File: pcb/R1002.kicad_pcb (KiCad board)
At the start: 2 copper layers, 45 x 33.3 mm, 11 parts, among them J1 PCIEXPRESS-X1, J2 CONN_01X04, J3 CONN_01X04, Q1 Q_NMOS_GDSD, Q2 Q_NMOS_GDSD, Q3 Q_NMOS_GDSD, Q4 Q_NMOS_GDSD, U1 MC14504B-TSSOP

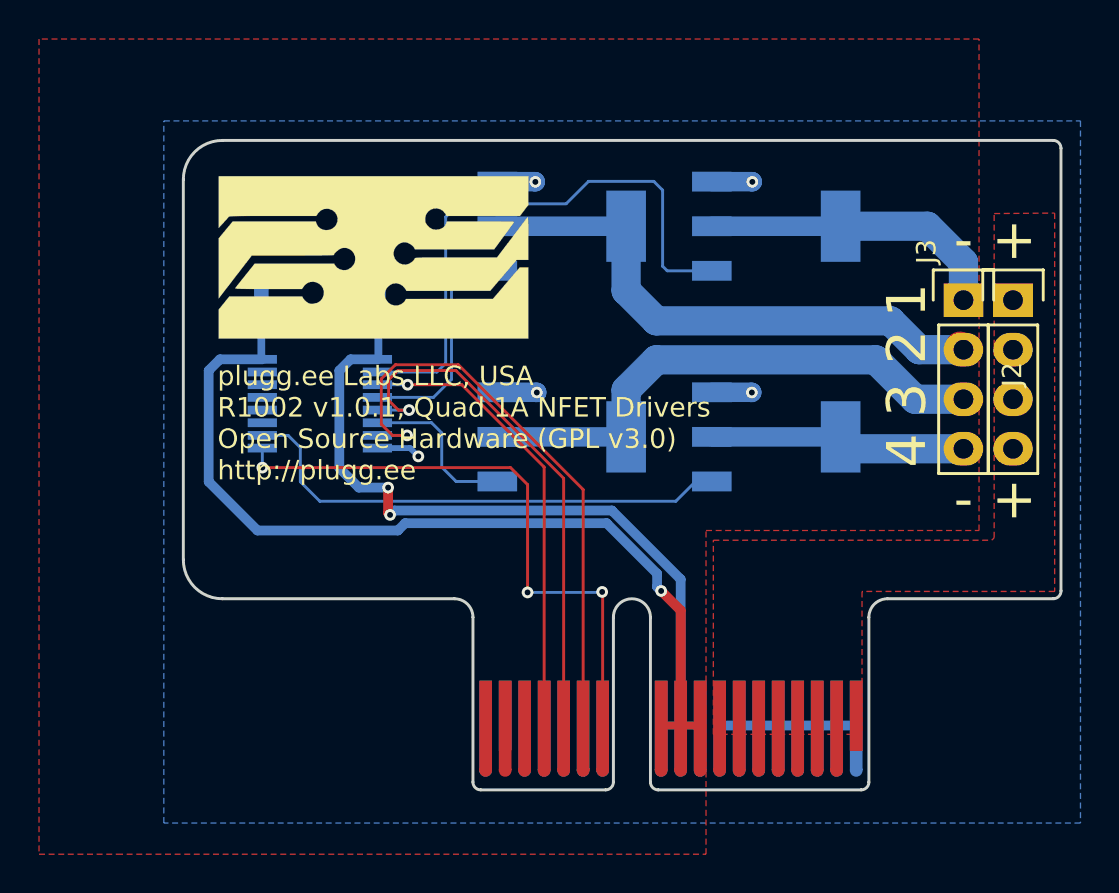
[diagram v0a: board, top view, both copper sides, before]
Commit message: added fiducials, exported BOM
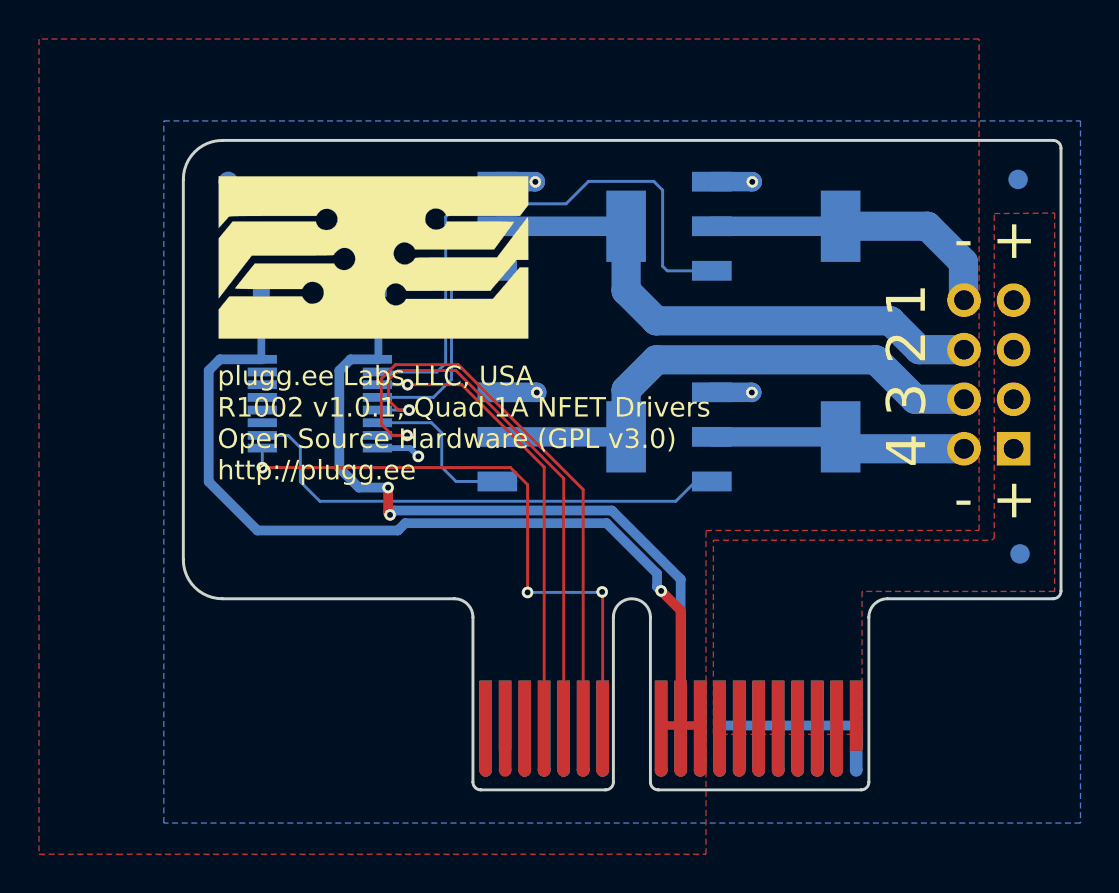
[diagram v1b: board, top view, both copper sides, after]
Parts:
- removed J3: CONN_01X04, Main:SOCKET254P-01X04
- added FID1: FIDTOP001, Main:FIDTOP001, B.Cu at (127.3, 72.1)
- added FID2: FIDTOP001, Main:FIDTOP001, B.Cu at (167.9, 91.2)
- added FID3: FIDTOP001, Main:FIDTOP001, B.Cu at (167.8, 72.0)
- C1, C3: value 0.1uF -> CC0603KRX7R9BB104; footprint Capacitors_SMD:C_0603 -> Main:CAPC0603
- J2: value CONN_01X04 -> CONN254P-02X04; footprint Main:SOCKET254P-01X04 -> Main:CONN254P-02X04; moved to B.Cu
- moved J2 1.30 mm to (166.3, 82.0), turned to 90 degrees
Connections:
- J2 pad 1: /DN1 -> HT
- J2 pad 2: /DN2 -> /DN4
- J2 pad 3: /DN3 -> HT
- J2 pad 4: /DN4 -> /DN3

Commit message: fixed silk screen with v1.1
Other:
- board text added: "plugg.ee Labs LLC, USA R1002 v1.1, Quad 1A NFET Drivers Open Source Hardware (GPL v3.0) http://plugg.ee"
- board text removed: "plugg.ee Labs LLC, USA R1002 v1.0.1, Quad 1A NFET Drivers Open Source Hardware (GPL v3.0) http://plugg.ee"
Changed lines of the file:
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@@
     (links 86)
     (no_connects 0)
-    (area 124.924999 69.924999 170.075001 103.375001)
+    (area 117.6 64.8 171.000001 106.600001)
     (thickness 1.6)
     (drawings 39)
@@
   (page A4)
   (layers
-    (0 F.Cu signal)
-    (31 B.Cu signal)
+    (0 F.Cu signal hide)
+    (31 B.Cu signal hide)
     (32 B.Adhes user)
     (33 F.Adhes user)
@@
     (35 F.Paste user)
     (36 B.SilkS user)
-    (37 F.SilkS user hide)
+    (37 F.SilkS user)
     (38 B.Mask user hide)
     (39 F.Mask user hide)
@@
     (effects (font (size 2 2) (thickness 0.2)) (justify mirror))
   )
-  (gr_text "plugg.ee Labs LLC, USA\nR1002 v1.0.1, Quad 1A NFET Drivers\nOpen Source Hardware (GPL v3.0)\nhttp://plugg.ee" (at 126.75 84.5) (layer F.SilkS)
+  (gr_text "plugg.ee Labs LLC, USA\nR1002 v1.1, Quad 1A NFET Drivers\nOpen Source Hardware (GPL v3.0)\nhttp://plugg.ee" (at 126.75 84.5) (layer F.SilkS)
     (effects (font (size 1 1) (thickness 0.2)) (justify left))
   )
